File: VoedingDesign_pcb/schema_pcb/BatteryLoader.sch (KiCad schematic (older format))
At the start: 1 part

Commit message: schema getekend (bijna af), nog pcb routing
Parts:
- added BT?: Battery_Cell, symbol Device:Battery_Cell
- added C? (x2): 10u, symbol Device:CP
- added C?: 0.1u, symbol Device:C
- added CBYP1: 0.1 uF, symbol Device:C
- added CIN1, CSTOR2: 4.7 uF, symbol Device:C
- added CREF2: 100 nF, symbol Device:C
- added J?: conn_meas_battery, symbol Connector:Conn_01x02_Female
- added J?: Conn_3V3, symbol Connector:Conn_01x20_Female
- added J?: Conn_GND, symbol Connector:Conn_01x20_Female
- added L?: 22 uH, symbol Device:L
- added ROK4, ROK5, ROK6, ROV3, ROV4: R, symbol Device:R
- added U?: NCP1117-3.3_SOT223, Package_TO_SOT_SMD:SOT-223-3_TabPin2, symbol Regulator_Linear:NCP1117-3.3_SOT223
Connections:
- net GND: now reaches U?.1 (VSS)
- net GND: now also U?.14 (VBAT_PRI), U?.15 (VSS), U?.16 (NC), U?.17 (NC), U?.5 (*EN), U?.6 (NC), BT?.2 (-), C?.2, C?.2, C?.2, CBYP1.2, CIN1.2, CREF2.2, CSTOR2.2, J?.1 (Pin_1), J?.10 (Pin_10), J?.11 (Pin_11), J?.12 (Pin_12), J?.13 (Pin_13), J?.14 (Pin_14), J?.15 (Pin_15), J?.16 (Pin_16), J?.17 (Pin_17), J?.18 (Pin_18), J?.19 (Pin_19), J?.2 (Pin_2), J?.2 (Pin_2), J?.20 (Pin_20), J?.3 (Pin_3), J?.4 (Pin_4), J?.5 (Pin_5), J?.6 (Pin_6), J?.7 (Pin_7), J?.8 (Pin_8), J?.9 (Pin_9), ROK4.2, ROV3.2, U?.1 (GND)
- net at U?.11 (OK_HYST): now also ROK5.1, ROK6.2
- net at U?.12 (OK_PROG): now also ROK4.1, ROK5.2
- net VBAT_SEC: now reaches U?.18 (VBAT_SEC)
- net VBAT_SEC: now also BT?.1 (+), J?.1 (Pin_1)
- net at U?.19 (VSTOR): now also U?.3 (VOC_SAMP), C?.1, CBYP1.1, CSTOR2.1, U?.3 (VI)
- net input: now reaches U?.2 (VIN_DC)
- net input: now also CIN1.1, L?.2
- net at U?.20 (LBOOST): now also L?.1
- net at U?.4 (VREF_SAMP): now also CREF2.1
- net at U?.7 (VBAT_OV): now also ROV3.1, ROV4.2
- net at U?.8 (VRDIV): now also ROK6.1, ROV4.1
- new net: C?.1, C?.1, J?.1 (Pin_1), J?.10 (Pin_10), J?.11 (Pin_11), J?.12 (Pin_12), J?.13 (Pin_13), J?.14 (Pin_14), J?.15 (Pin_15), J?.16 (Pin_16), J?.17 (Pin_17), J?.18 (Pin_18), J?.19 (Pin_19), J?.2 (Pin_2), J?.20 (Pin_20), J?.3 (Pin_3), J?.4 (Pin_4), J?.5 (Pin_5), J?.6 (Pin_6), J?.7 (Pin_7), J?.8 (Pin_8), J?.9 (Pin_9), U?.2 (VO)
- no-connect marks 0 -> 4
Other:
- moved on the sheet: U?

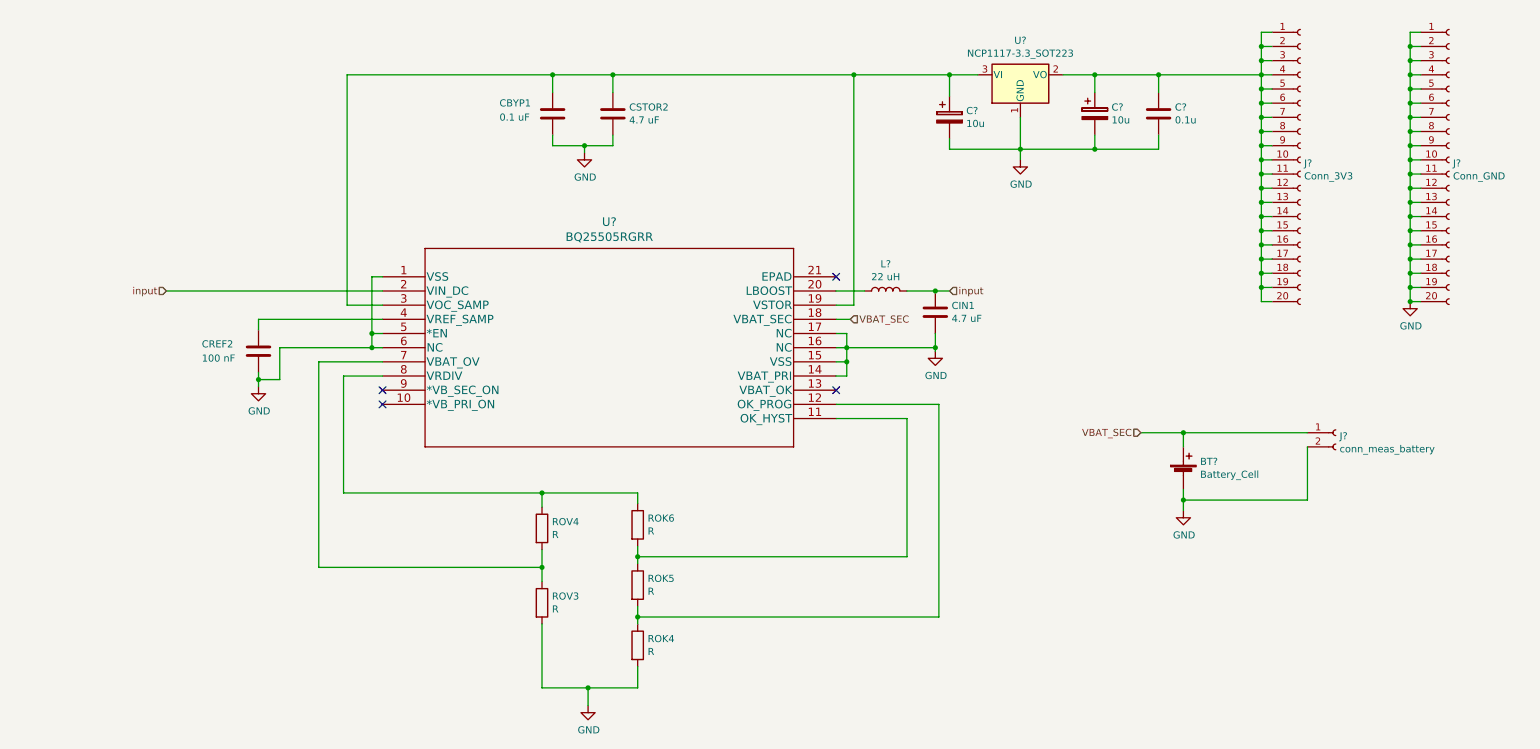
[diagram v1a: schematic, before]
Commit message: schema getekend voeding_ bijna alle footprints volledig
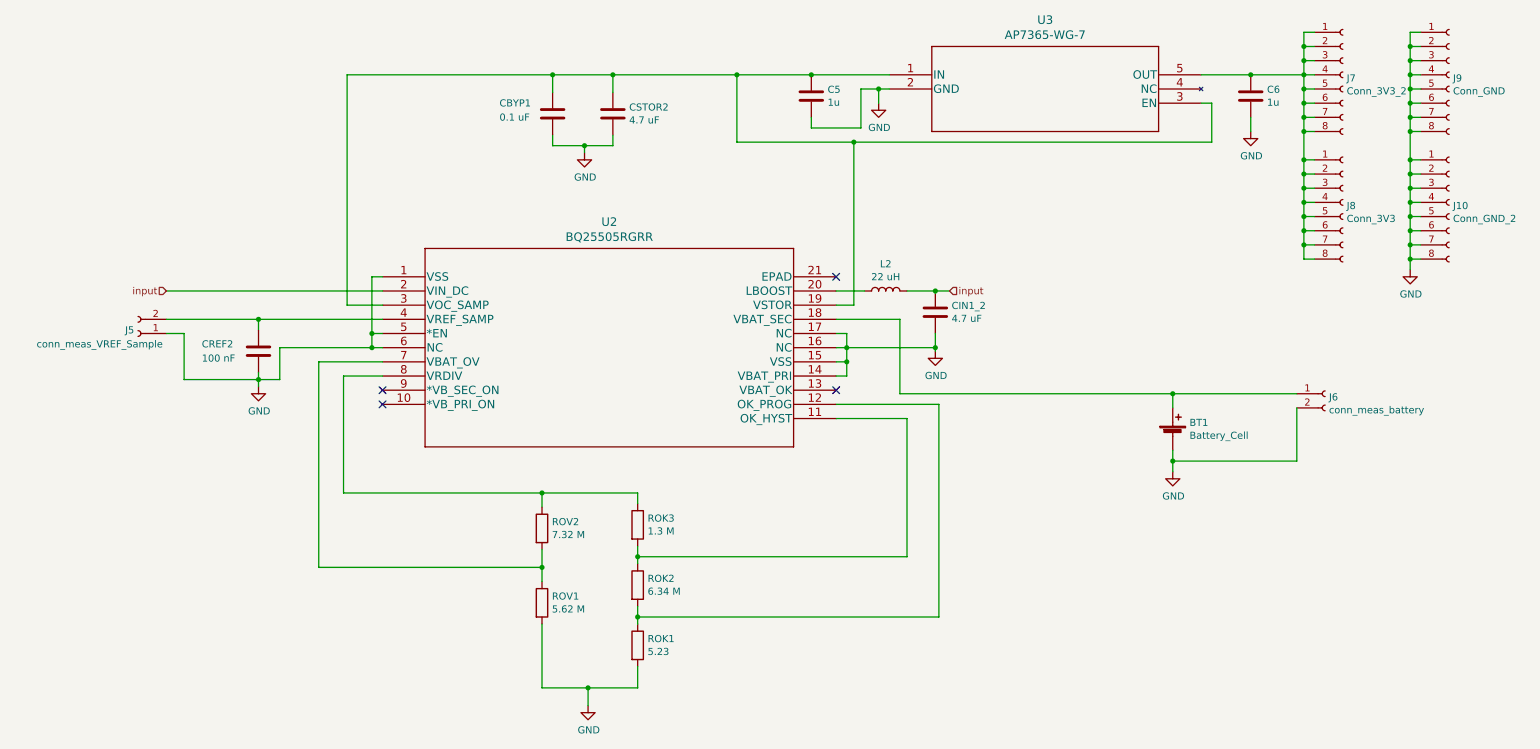
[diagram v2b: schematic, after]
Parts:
- removed C? (x2): 10u, symbol Device:CP
- removed J?: Conn_3V3, symbol Connector:Conn_01x20_Female
- removed J?: Conn_GND, symbol Connector:Conn_01x20_Female
- removed U?: NCP1117-3.3_SOT223, Package_TO_SOT_SMD:SOT-223-3_TabPin2, symbol Regulator_Linear:NCP1117-3.3_SOT223
- added C5: 1u, Capacitor_SMD:C_0603_1608Metric_Pad1.05x0.95mm_HandSolder, symbol Device:C
- added J10: Conn_GND_2, Connector_PinHeader_2.54mm:PinHeader_1x08_P2.54mm_Vertical, symbol Connector:Conn_01x08_Female
- added J5: conn_meas_VREF_Sample, Connector_PinHeader_2.54mm:PinHeader_1x02_P2.54mm_Vertical, symbol Connector:Conn_01x02_Female
- added J7: Conn_3V3_2, Connector_PinHeader_2.54mm:PinHeader_1x08_P2.54mm_Vertical, symbol Connector:Conn_01x08_Female
- added J8: Conn_3V3, Connector_PinHeader_2.54mm:PinHeader_1x08_P2.54mm_Vertical, symbol Connector:Conn_01x08_Female
- added J9: Conn_GND, Connector_PinHeader_2.54mm:PinHeader_1x08_P2.54mm_Vertical, symbol Connector:Conn_01x08_Female
- added U3: AP7365-WG-7, extraFootprints:AP7365-WG-7, symbol AP7365:AP7365-WG-7
- BT1: renamed from BT?; footprint (none) -> Connector_PinHeader_2.54mm:PinHeader_1x02_P2.54mm_Vertical
- C6: renamed from C?; value 0.1u -> 1u; footprint (none) -> Capacitor_SMD:C_0603_1608Metric_Pad1.05x0.95mm_HandSolder
- CBYP1, CREF2: footprint (none) -> Capacitor_SMD:C_0805_2012Metric_Pad1.15x1.40mm_HandSolder
- CIN1_2: renamed from CIN1; footprint (none) -> Capacitor_SMD:C_0805_2012Metric_Pad1.15x1.40mm_HandSolder
- J6: renamed from J?; footprint (none) -> Connector_PinHeader_2.54mm:PinHeader_1x02_P2.54mm_Vertical
- ROK1: renamed from ROK4; value R -> 5.23; footprint (none) -> Resistor_SMD:R_1206_3216Metric_Pad1.42x1.75mm_HandSolder
- ROK2: renamed from ROK5; value R -> 6.34 M; footprint (none) -> Resistor_SMD:R_0805_2012Metric_Pad1.15x1.40mm_HandSolder
- ROK3: renamed from ROK6; value R -> 1.3 M; footprint (none) -> Resistor_SMD:R_1206_3216Metric_Pad1.42x1.75mm_HandSolder
- ROV1: renamed from ROV3; value R -> 5.62 M; footprint (none) -> Resistor_SMD:R_1206_3216Metric_Pad1.42x1.75mm_HandSolder
- ROV2: renamed from ROV4; value R -> 7.32 M; footprint (none) -> Resistor_SMD:R_0805_2012Metric_Pad1.15x1.40mm_HandSolder
- U2: renamed from U?; footprint RGR20_2P05X2P05 -> extraFootprints:BQ25505RGRR
- gave numbers to parts that had none: 1
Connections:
- net GND: now also C5.2, J10.1 (Pin_1), J10.2 (Pin_2), J10.3 (Pin_3), J10.4 (Pin_4), J10.5 (Pin_5), J10.6 (Pin_6), J10.7 (Pin_7), J10.8 (Pin_8), J5.1 (Pin_1), J9.1 (Pin_1), J9.2 (Pin_2), J9.3 (Pin_3), J9.4 (Pin_4), J9.5 (Pin_5), J9.6 (Pin_6), J9.7 (Pin_7), J9.8 (Pin_8), U3.2 (GND)
- net at CBYP1.1, CSTOR2.1, U2.19 (VSTOR)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: now also C5.1, U3.1 (IN), U3.3 (EN)
- net at CREF2.1, U2.4 (VREF_SAMP): now also J5.2 (Pin_2)
- net at C6.1: now also J7.1 (Pin_1), J7.2 (Pin_2), J7.3 (Pin_3), J7.4 (Pin_4), J7.5 (Pin_5), J7.6 (Pin_6), J7.7 (Pin_7), J7.8 (Pin_8), J8.1 (Pin_1), J8.2 (Pin_2), J8.3 (Pin_3), J8.4 (Pin_4), J8.5 (Pin_5), J8.6 (Pin_6), J8.7 (Pin_7), J8.8 (Pin_8), U3.5 (OUT)
- net VBAT_SEC: no longer names the net of BT1.1 (+), J6.1 (Pin_1), U2.18 (VBAT_SEC)
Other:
- moved on the sheet: BT1, C6, J6

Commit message: afgewerkte Energy Harvesting PCB
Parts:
- CIN1_2: footprint Capacitor_SMD:C_0805_2012Metric_Pad1.15x1.40mm_HandSolder -> Capacitor_SMD:CP_Elec_6.3x5.3
- CSTOR2: footprint (none) -> Capacitor_SMD:CP_Elec_6.3x5.3
- L2: footprint (none) -> Inductor_SMD:L_Coilcraft_XxL4040
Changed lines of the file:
@@
 F 0 "CIN1_2" H 6865 2821 50  0000 L CNN
 F 1 "4.7 uF" H 6865 2730 50  0000 L CNN
-F 2 "Capacitor_SMD:C_0805_2012Metric_Pad1.15x1.40mm_HandSolder" H 6788 2625 50  0001 C CNN
+F 2 "Capacitor_SMD:CP_Elec_6.3x5.3" H 6788 2625 50  0001 C CNN
 F 3 "~" H 6750 2775 50  0001 C CNN
 	1    6750 2775
@@
 F 0 "L2" V 6590 2625 50  0000 C CNN
 F 1 "22 uH" V 6499 2625 50  0000 C CNN
-F 2 "" H 6400 2625 50  0001 C CNN
+F 2 "Inductor_SMD:L_Coilcraft_XxL4040" H 6400 2625 50  0001 C CNN
 F 3 "~" H 6400 2625 50  0001 C CNN
 	1    6400 2625
@@
 F 0 "CSTOR2" H 4590 1421 50  0000 L CNN
 F 1 "4.7 uF" H 4590 1330 50  0000 L CNN
-F 2 "" H 4513 1225 50  0001 C CNN
+F 2 "Capacitor_SMD:CP_Elec_6.3x5.3" H 4513 1225 50  0001 C CNN
 F 3 "~" H 4475 1375 50  0001 C CNN
 	1    4475 1375
